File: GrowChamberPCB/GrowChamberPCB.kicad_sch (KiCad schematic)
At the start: 7 parts, among them CN2 RelayBoard Interconnect, P1 12V_In, U4 To Faceplate, U6 CR2013-MI2120

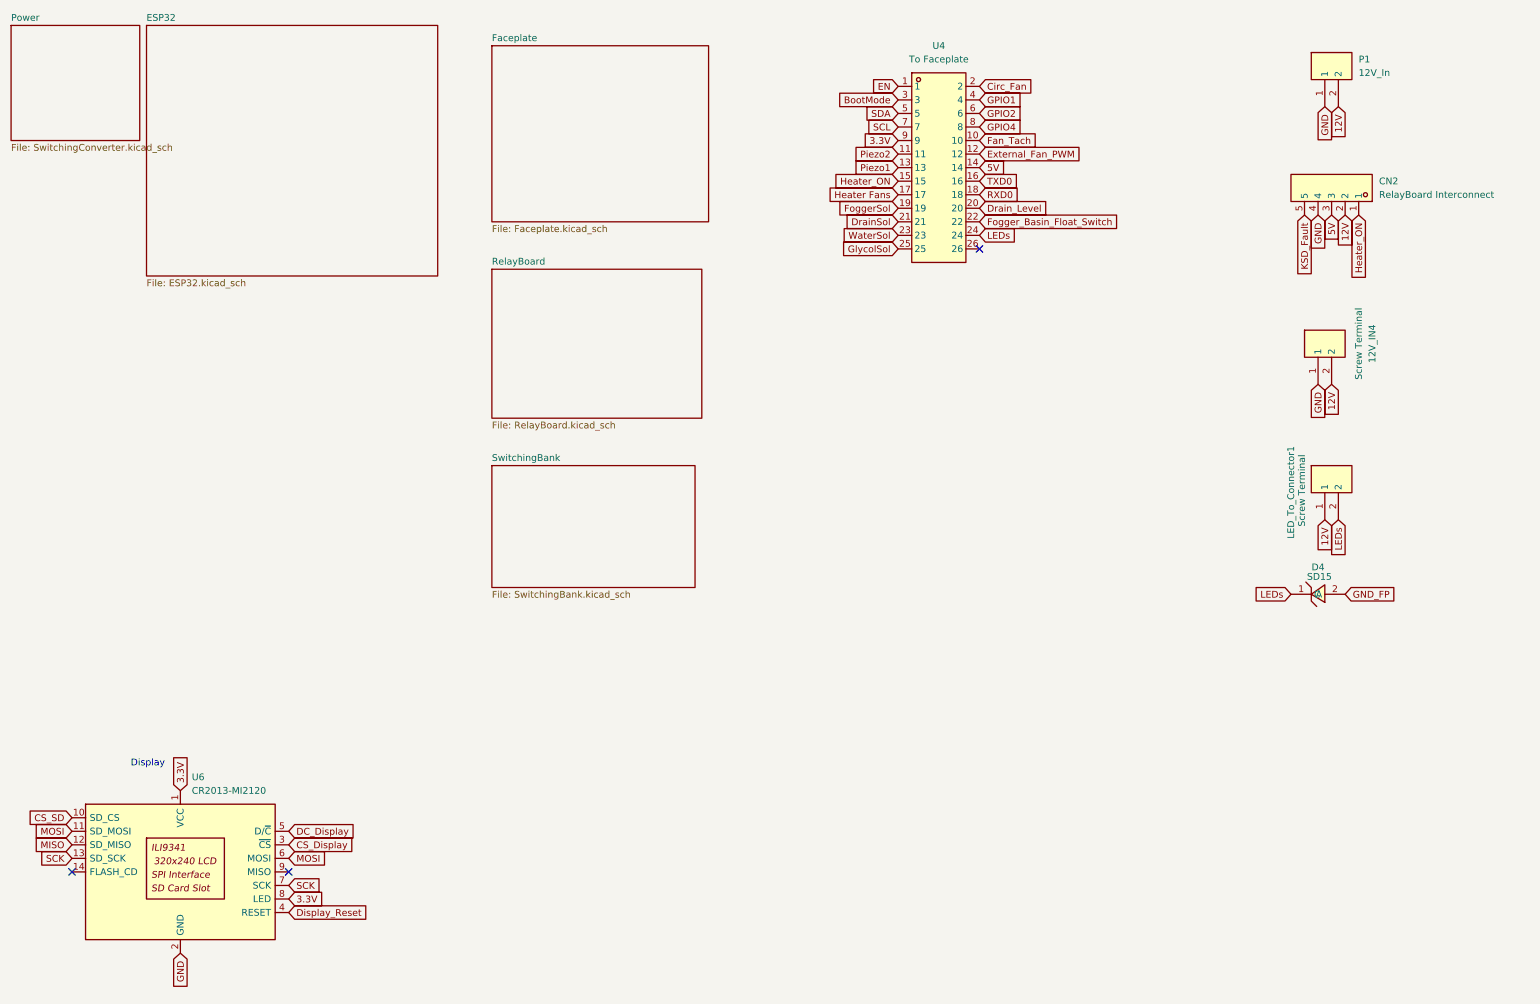
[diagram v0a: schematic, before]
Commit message: Removed 3.3V, wired some stuff
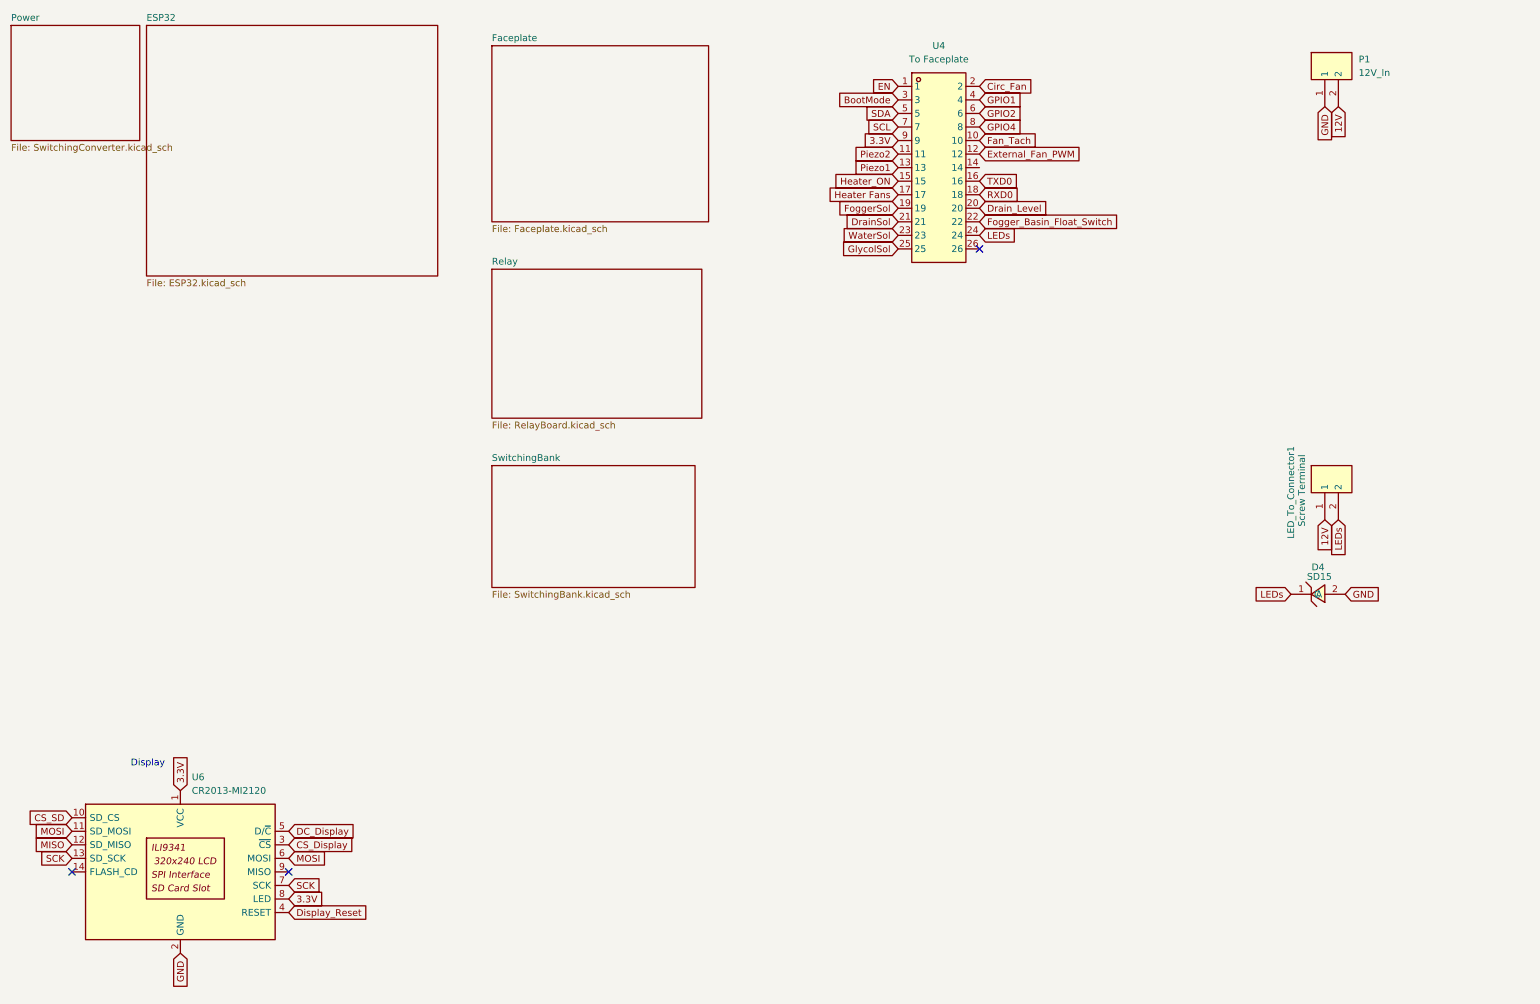
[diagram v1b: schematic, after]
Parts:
- removed 12V_IN4: Screw Terminal, easyeda2kicad:CONN-TH_2P-P5.00_CPC3703CTR, symbol easyeda2kicad:WJ127-5.0-2P
- removed CN2: RelayBoard Interconnect, easyeda2kicad:CONN-TH_5P-P5.00_WJ127-5.0-5P, symbol easyeda2kicad:WJ127-5.0-5P
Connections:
- net GND_FP is gone; now on net GND: D4.2 (A)
- net 5V: no longer names the net of U4.14
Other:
- sheet RelayBoard renamed Relay

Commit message: failing to route the board
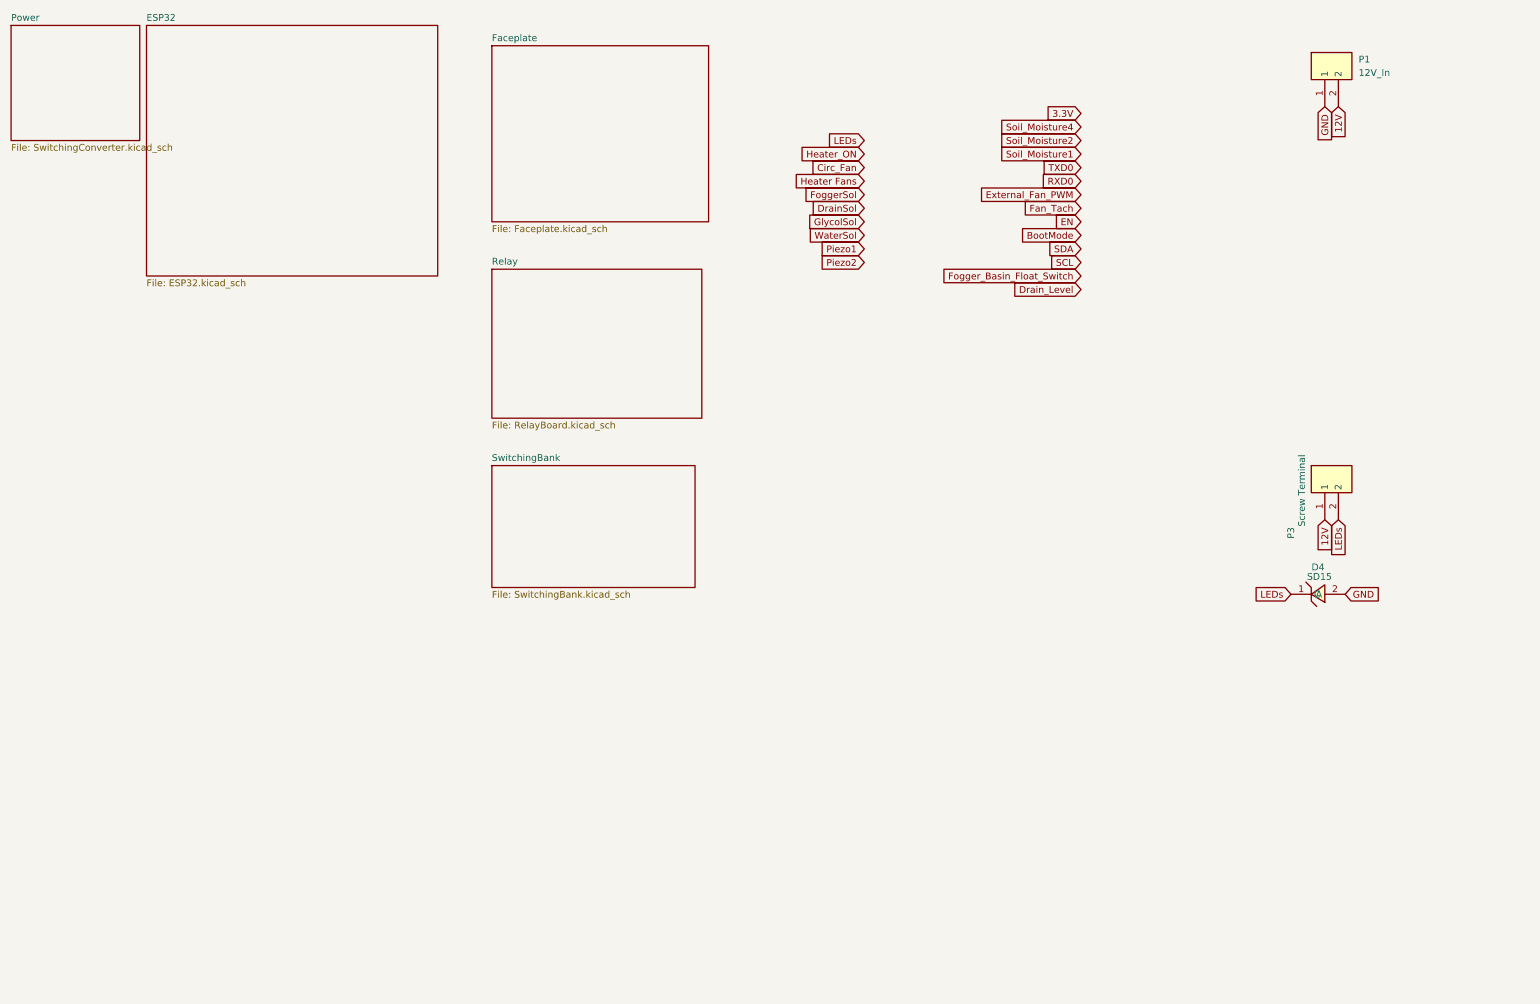
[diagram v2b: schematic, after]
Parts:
- removed U4: To Faceplate, easyeda2kicad:IDC-TH_26P-P2.54_ZX-IDC2.54-2-13PZZ, symbol easyeda2kicad:ZX-IDC2.54-2-13PZZ
- removed U6: CR2013-MI2120, Connector_PinHeader_2.54mm:PinHeader_1x14_P2.54mm_Vertical, symbol Driver_Display:CR2013-MI2120
- renumbered LED_To_Connector1 to P3
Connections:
- no-connect marks 3 -> 0
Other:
- note removed: "Display"

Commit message: redesign 3
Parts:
- added U4: ZX-IDC2.54-2-13PZZ, easyeda2kicad:IDC-TH_26P-P2.54_ZX-IDC2.54-2-13PZZ, symbol easyeda2kicad:ZX-IDC2.54-2-13PZZ
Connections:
- net LEDs: now also U4.7
- new net 3.3V: U4.2, U4.4
- new net BootMode: U4.8
- new net Circ_Fan: U4.19
- new net DrainSol: U4.17
- new net Drain_Level: U4.16
- new net EN: U4.6
- new net External_Fan_PWM: U4.24
- new net Fan_Tach: U4.26
- new net FoggerSol: U4.13
- new net Fogger_Basin_Float_Switch: U4.18
- new net GlycolSol: U4.11
- new net Heater Fans: U4.15
- new net Heater_ON: U4.5
- new net Piezo1: U4.3
- new net Piezo2: U4.1
- new net RXD0: U4.20
- new net SCL: U4.25
- new net SDA: U4.23
- new net Soil_Moisture1: U4.14
- new net Soil_Moisture2: U4.12
- new net Soil_Moisture4: U4.10
- new net TXD0: U4.22
- new net WaterSol: U4.9
- no-connect marks 0 -> 1

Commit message: finished routing
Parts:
- P1: now not fitted
- P3: value Screw Terminal -> LED Connector; now not fitted
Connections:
- net 3.3V: now also U4.18, U4.20; no longer U4.2, U4.4
- net Circ_Fan: now also U4.24; no longer U4.19
- net DrainSol: now also U4.19; no longer U4.17
- net Drain_Level: now also U4.6; no longer U4.16
- net EN: now also U4.2; no longer U4.6
- net External_Fan_PWM: now also U4.25; no longer U4.24
- net Fan_Tach: now also U4.23; no longer U4.26
- net FoggerSol: now also U4.21; no longer U4.13
- net Fogger_Basin_Float_Switch: now also U4.4; no longer U4.18
- net GlycolSol: now also U4.17; no longer U4.11
- net Heater Fans: now also U4.22; no longer U4.15
- net Heater_ON: now also U4.1; no longer U4.5
- net LEDs: now also U4.3; no longer U4.7
- net Piezo1: now also U4.7; no longer U4.3
- net Piezo2: now also U4.5; no longer U4.1
- net RXD0: now also U4.10; no longer U4.20
- net SCL: now also U4.11; no longer U4.25
- net SDA: now also U4.12; no longer U4.23
- net Soil_Moisture2: now also U4.15; no longer U4.12
- net Soil_Moisture4: now also U4.13; no longer U4.10
- net TXD0: now also U4.9; no longer U4.22
- net WaterSol: now also U4.16; no longer U4.9
- new net Heartbeat_LED: U4.26
- no-connect marks 1 -> 0
